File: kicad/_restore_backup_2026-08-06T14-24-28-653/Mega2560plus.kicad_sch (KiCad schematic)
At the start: 6 parts

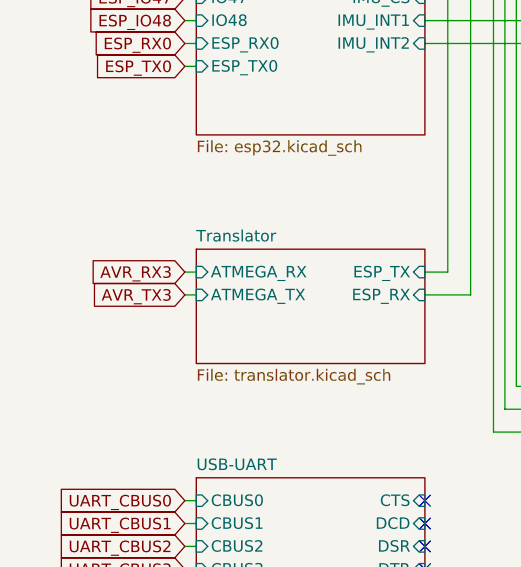
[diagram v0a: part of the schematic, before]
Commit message: fix silkscreen
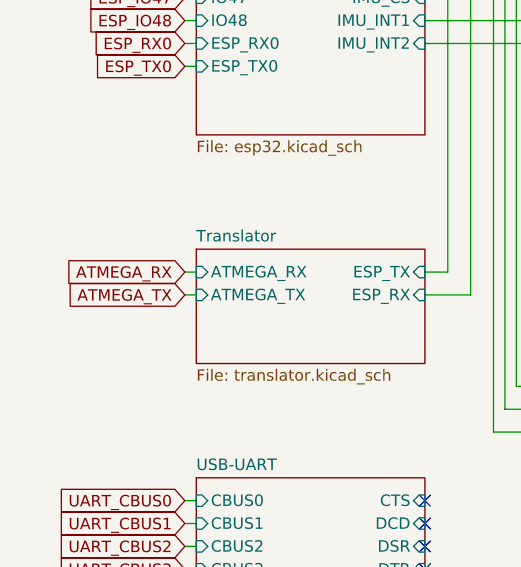
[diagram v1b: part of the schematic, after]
